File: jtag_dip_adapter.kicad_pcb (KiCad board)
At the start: 2 copper layers, 21.3 x 78.5 mm, 22 parts, among them J1 USB_B_Micro, J2 Conn_01x22, J3 Conn_01x22, J4 JTAG, J5 Conn_01x02, U1 MAX40203AUK+T, U2 74LVC1G04

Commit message: initial layout
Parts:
- added D3: BAT54W, Package_TO_SOT_SMD:SOT-323_SC-70, F.Cu at (134.1, 117.6)
- U2: value 74LVC1G04 -> 74HCT1G04
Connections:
- J5 pad 1: VCC -> Net-(D3-Pad1)
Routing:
- net VCC: track 0.00 -> 72.6 mm
- added copper zone on B.Cu, net GND
- added copper zone on F.Cu, net GND
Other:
- net class Default: clearance 0.2 -> 0.254; trace_width 0.25 -> 0.254; via_dia 0.8 -> 0.508; via_drill 0.4 -> 0.254
- net class Power added: clearance 0.254, trace_width 0.4064, via_dia 0.8128, via_drill 0.4064
- rule trace_clearance: 0.2 -> 0.254
- rule trace_min: 0.2 -> 0.1524
- rule via_min_drill: 0.3 -> 0.254
- rule via_min_size: 0.4 -> 0.508
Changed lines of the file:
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@@
     (thickness 1.6)
     (drawings 4)
-    (tracks 0)
+    (tracks 4)
     (zones 0)
-    (modules 22)
-    (nets 12)
+    (modules 23)
+    (nets 13)
   )
   (page A4)
@@
   )
   (setup
-    (last_trace_width 0.25)
-    (trace_clearance 0.2)
+    (last_trace_width 0.254)
+    (user_trace_width 0.254)
+    (user_trace_width 0.4064)
+    (trace_clearance 0.254)
     (zone_clearance 0.508)
     (zone_45_only no)
-    (trace_min 0.2)
-    (via_size 0.8)
-    (via_drill 0.4)
-    (via_min_size 0.4)
-    (via_min_drill 0.3)
+    (trace_min 0.1524)
+    (via_size 0.508)
+    (via_drill 0.254)
+    (via_min_size 0.508)
+    (via_min_drill 0.254)
+    (user_via 0.508 0.254)
+    (user_via 0.8128 0.4064)
     (uvia_size 0.3)
     (uvia_drill 0.1)
@@
     (pcb_text_width 0.3)
     (pcb_text_size 1.5 1.5)
-    (mod_edge_width 0.12)
-    (mod_text_size 1 1)
-    (mod_text_width 0.15)
+    (mod_edge_width 0.1524)
+    (mod_text_size 0.8128 0.8128)
+    (mod_text_width 0.1524)
     (pad_size 1.524 1.524)
     (pad_drill 0.762)
@@
   (net 10 /TCK)
   (net 11 /TDO)
+  (net 12 "Net-(D3-Pad1)")
   (net_class Default "This is the default net class."
-    (clearance 0.2)
-    (trace_width 0.25)
-    (via_dia 0.8)
-    (via_drill 0.4)
+    (clearance 0.254)
+    (trace_width 0.254)
+    (via_dia 0.508)
+    (via_drill 0.254)
     (uvia_dia 0.3)
     (uvia_drill 0.1)
@@
     (add_net /TDO)
     (add_net /TMS)
-    (add_net GND)
     (add_net "Net-(C1-Pad1)")
     (add_net "Net-(C3-Pad1)")
@@
     (add_net "Net-(D2-Pad1)")
     (add_net "Net-(D2-Pad2)")
+    (add_net "Net-(D3-Pad1)")
     (add_net "Net-(J1-Pad2)")
     (add_net "Net-(J1-Pad3)")
@@
     (add_net "Net-(J4-Pad8)")
     (add_net "Net-(U1-Pad4)")
+  )
+  (net_class Power ""
+    (clearance 0.254)
+    (trace_width 0.4064)
+    (via_dia 0.8128)
+    (via_drill 0.4064)
+    (uvia_dia 0.3)
+    (uvia_drill 0.1)
+    (add_net GND)
     (add_net VCC)
+  )
+  (module Package_TO_SOT_SMD:SOT-323_SC-70 (layer F.Cu)
+    (at 134.112 117.602)
+    (descr "SOT-323, SC-70")
+    (tags "SOT-323 SC-70")
+    (attr smd)
+    (fp_text reference D3 (at -0.05 -1.95) (layer F.SilkS)
+      (effects (font (size 1 1) (thickness 0.15)))
+    )
+    (fp_text value BAT54W (at -0.05 2.05) (layer F.Fab)
+      (effects (font (size 1 1) (thickness 0.15)))
+    )
+    (fp_line (start -0.18 -1.1) (end -0.68 -0.6) (layer F.Fab) (width 0.1))
+    (fp_line (start 0.67 1.1) (end -0.68 1.1) (layer F.Fab) (width 0.1))
+    (fp_line (start 0.67 -1.1) (end 0.67 1.1) (layer F.Fab) (width 0.1))
+    (fp_line (start -0.68 -0.6) (end -0.68 1.1) (layer F.Fab) (width 0.1))
+    (fp_line (start 0.67 -1.1) (end -0.18 -1.1) (layer F.Fab) (width 0.1))
+    (fp_line (start -0.68 1.16) (end 0.73 1.16) (layer F.SilkS) (width 0.12))
+    (fp_line (start 0.73 -1.16) (end -1.3 -1.16) (layer F.SilkS) (width 0.12))
+    (fp_line (start -1.7 1.3) (end -1.7 -1.3) (layer F.CrtYd) (width 0.05))
+    (fp_line (start -1.7 -1.3) (end 1.7 -1.3) (layer F.CrtYd) (width 0.05))
+    (fp_line (start 1.7 -1.3) (end 1.7 1.3) (layer F.CrtYd) (width 0.05))
+    (fp_line (start 1.7 1.3) (end -1.7 1.3) (layer F.CrtYd) (width 0.05))
+    (fp_line (start 0.73 -1.16) (end 0.73 -0.5) (layer F.SilkS) (width 0.12))
+    (fp_line (start 0.73 0.5) (end 0.73 1.16) (layer F.SilkS) (width 0.12))
+    (fp_text user %R (at 0 0 90) (layer F.Fab)
+      (effects (font (size 0.5 0.5) (thickness 0.075)))
+    )
+    (pad 3 smd rect (at 1 0 270) (size 0.45 0.7) (layers F.Cu F.Paste F.Mask)
+      (net 4 VCC))
+    (pad 2 smd rect (at -1 0.65 270) (size 0.45 0.7) (layers F.Cu F.Paste F.Mask))
+    (pad 1 smd rect (at -1 -0.65 270) (size 0.45 0.7) (layers F.Cu F.Paste F.Mask)
+      (net 12 "Net-(D3-Pad1)"))
+    (model ${KISYS3DMOD}/Package_TO_SOT_SMD.3dshapes/SOT-323_SC-70.wrl
+      (at (xyz 0 0 0))
+      (scale (xyz 1 1 1))
+      (rotate (xyz 0 0 0))
+    )
   )
   (module Connector_PinHeader_2.54mm:PinHeader_1x02_P2.54mm_Horizontal (layer F.Cu)
@@
       (net 1 GND))
     (pad 1 thru_hole rect (at 0 0 180) (size 1.7 1.7) (drill 1) (layers *.Cu *.Mask)
-      (net 4 VCC))
+      (net 12 "Net-(D3-Pad1)"))
     (model ${KISYS3DMOD}/Connector_PinHeader_2.54mm.3dshapes/PinHeader_1x02_P2.54mm_Horizontal.wrl
       (at (xyz 0 0 0))
@@
       (effects (font (size 1 1) (thickness 0.15)))
     )
-    (fp_text value 74LVC1G04 (at 0 2.5) (layer F.Fab)
+    (fp_text value 74HCT1G04 (at 0 2.5) (layer F.Fab)
       (effects (font (size 1 1) (thickness 0.15)))
     )
@@
   (gr_line (start 127 55.118) (end 148.336 55.118) (layer Edge.Cuts) (width 0.05))
   (gr_line (start 127 133.604) (end 127 55.118) (layer Edge.Cuts) (width 0.05))
+  (segment (start 130.048 77.724) (end 128.016 77.724) (width 0.4064) (layer F.Cu) (net 4))
+  (segment (start 128.016 77.724) (end 128.016 55.88) (width 0.4064) (layer F.Cu) (net 4))
+  (segment (start 128.016 77.724) (end 128.016 96.012) (width 0.4064) (layer F.Cu) (net 4))
+  (segment (start 128.016 96.012) (end 128.016 126.492) (width 0.4064) (layer F.Cu) (net 4))
+  (zone (net 1) (net_name GND) (layer F.Cu) (hatch edge 0.508)
+    (connect_pads (clearance 0.508))
+    (min_thickness 0.254)
+    (fill (arc_segments 32) (thermal_gap 0.508) (thermal_bridge_width 0.508))
+    (polygon
+      (pts
+        (xy 127 55.118) (xy 148.336 55.118) (xy 148.336 133.604) (xy 127 133.604)
+      )
+    )
+  )
+  (zone (net 1) (net_name GND) (layer B.Cu) (hatch edge 0.508)
+    (connect_pads (clearance 0.508))
+    (min_thickness 0.254)
+    (fill (arc_segments 32) (thermal_gap 0.508) (thermal_bridge_width 0.508))
+    (polygon
+      (pts
+        (xy 127 55.118) (xy 148.336 55.118) (xy 148.336 133.604) (xy 127.508 133.604) (xy 127 133.604)
+      )
+    )
+  )
 )

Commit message: finished routing and silkscreen
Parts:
- C1, C2, C4, C5, C6, C7, C8, D3, R3, U1, U2: moved to B.Cu
- moved D2 4.08 mm to (145.3, 121.2)
- moved R5 3.98 mm to (141.5, 121.2), turned to 180 degrees
- moved D3 3.57 mm to (133.9, 114.0)
- moved C1 3.30 mm to (134.1, 70.1)
- moved U2 2.97 mm to (142.5, 117.1)
- moved C2 2.40 mm to (141.5, 70.1)
- moved U1 2.34 mm to (137.2, 67.3)
- moved C4 2.30 mm to (133.9, 125.2)
- moved R1 1.41 mm to (140.2, 62.7)
- moved C3 1.02 mm to (135.1, 62.7)
- moved C8 0.29 mm to (141.5, 64.8)
- moved C6 0.25 mm to (133.9, 98.0)
- moved R2 0.25 mm to (133.9, 121.2)
- moved C7 0.14 mm to (141.5, 95.5)
- moved R4 0.14 mm to (141.5, 103.1)
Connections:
- J5 pad 1: Net-(D3-Pad1) -> GND
- J5 pad 2: GND -> Net-(D3-Pad1)
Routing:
- net /TDI: track 0.00 -> 80.7 mm, vias 0 -> 1
- net /TMS: track 0.00 -> 64.0 mm
- net /TDO: track 0.00 -> 55.7 mm
- net VCC: track 72.6 -> 126.2 mm, vias 0 -> 1
- net /TCK: track 0.00 -> 46.3 mm, vias 0 -> 2
- net GND: track 0.00 -> 22.9 mm, vias 0 -> 22
- net Net-(C3-Pad1): track 0.00 -> 17.2 mm
- net Net-(C1-Pad1): track 0.00 -> 14.5 mm, vias 0 -> 1
- net Net-(D2-Pad2): track 0.00 -> 6.81 mm, vias 0 -> 1
- net Net-(D3-Pad1): track 0.00 -> 2.87 mm
- net Net-(D2-Pad1): track 0.00 -> 2.06 mm
- net Net-(D1-Pad2): track 0.00 -> 2.06 mm
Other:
- rule pad_to_mask_clearance: 0.051 -> 0.0508
- rule solder_mask_min_width: 0.25 -> 0.1016
- board text added: "+5V"
- board text added: "1"
- board text added: "For 44 pin QFP and PLCC devices only with DIP adapter"
- board text added: "GND"
- board text added: "JTAG"
- board text added: "MAX7000S JTAG Adapter v1.0 by Hyiger Designs"
- board text added: "PWR"

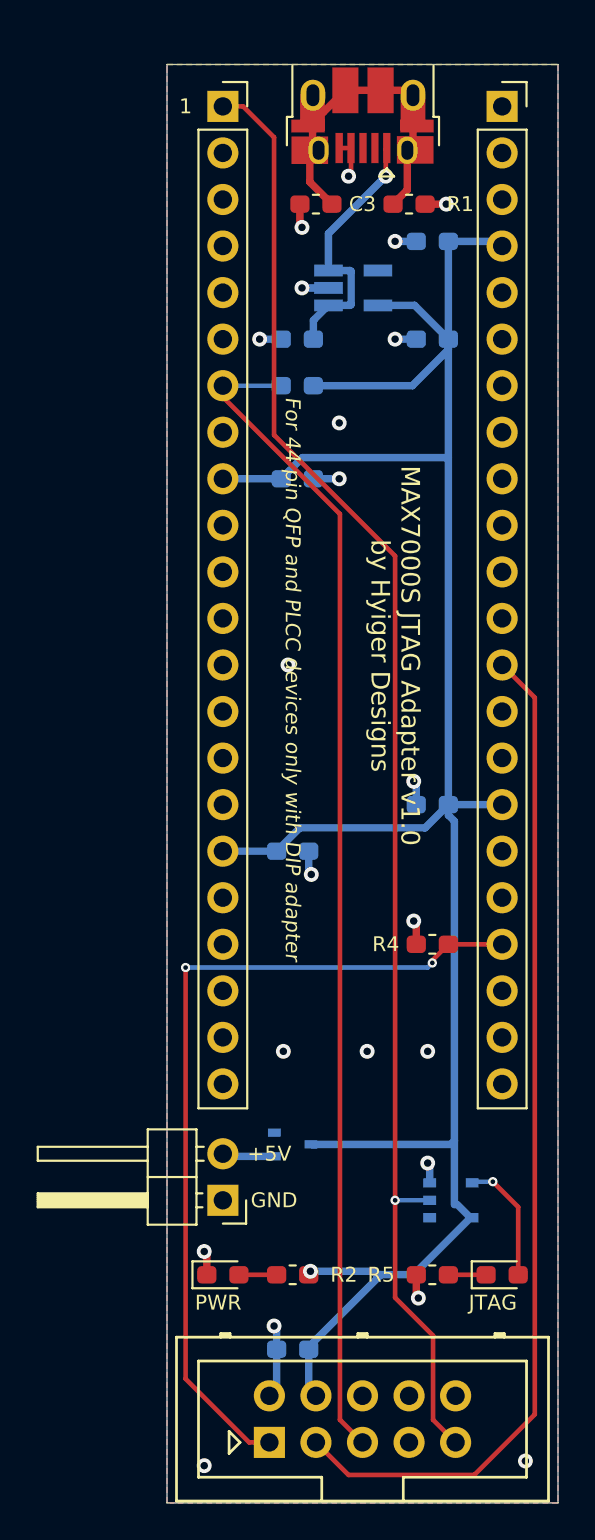
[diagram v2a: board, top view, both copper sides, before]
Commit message: added 5V ldo reg
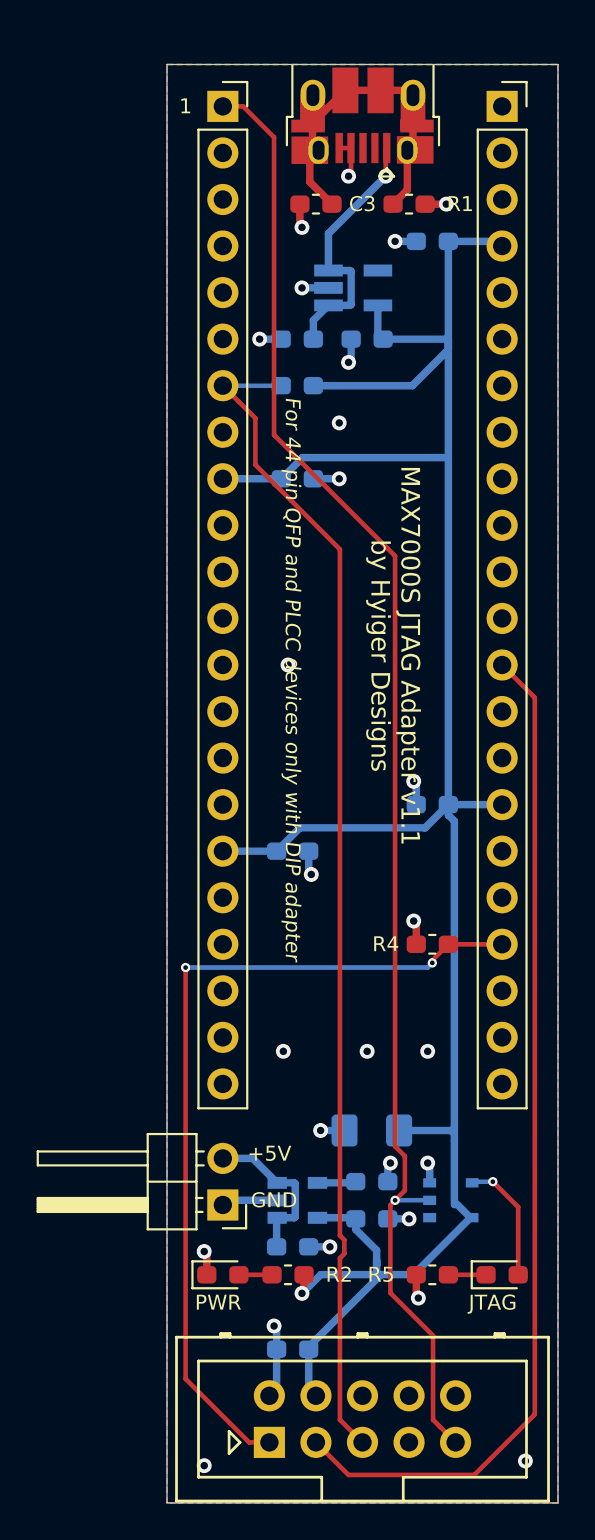
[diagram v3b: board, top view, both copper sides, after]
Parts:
- removed D3: BAT54W, Package_TO_SOT_SMD:SOT-323_SC-70
- removed J5: Conn_01x02, Connector_PinHeader_2.54mm:PinHeader_1x02_P2.54mm_Horizontal
- added C10: 10nF, Capacitor_SMD:C_0603_1608Metric_Pad1.05x0.95mm_HandSolder, B.Cu at (138.2, 116.1)
- added C11: 2.2uF, Capacitor_SMD:C_0603_1608Metric_Pad1.05x0.95mm_HandSolder, B.Cu at (138.2, 118.1)
- added C12: 100uF, Capacitor_SMD:C_1206_3216Metric_Pad1.42x1.75mm_HandSolder, B.Cu at (138.2, 113.3)
- added C9: 1uF, Capacitor_SMD:C_0603_1608Metric_Pad1.05x0.95mm_HandSolder, B.Cu at (133.9, 119.6)
- added J6: PWR, Connector_PinHeader_2.54mm:PinHeader_1x02_P2.54mm_Horizontal, F.Cu at (130.0, 117.3)
- added U3: LP2985-5.0, Package_TO_SOT_SMD:SOT-23-5, B.Cu at (134.1, 117.1)
- moved C2 3.56 mm to (137.9, 70.1)
- moved R2 0.25 mm to (133.6, 121.2)
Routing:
- net Net-(C9-Pad1): track 0.00 -> 9.14 mm
- net GND: track 22.9 -> 30.8 mm, vias 22 -> 26
- net VCC: track 126.2 -> 130.1 mm
- net Net-(D3-Pad1): track 2.87 -> 0.00 mm
- net Net-(C10-Pad1): track 0.00 -> 2.12 mm
- net /TDI: track 80.7 -> 81.3 mm
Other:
- board text added: "MAX7000S JTAG Adapter v1.1 by Hyiger Designs"
- board text removed: "MAX7000S JTAG Adapter v1.0 by Hyiger Designs"

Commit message: removed extra capacitor and vias
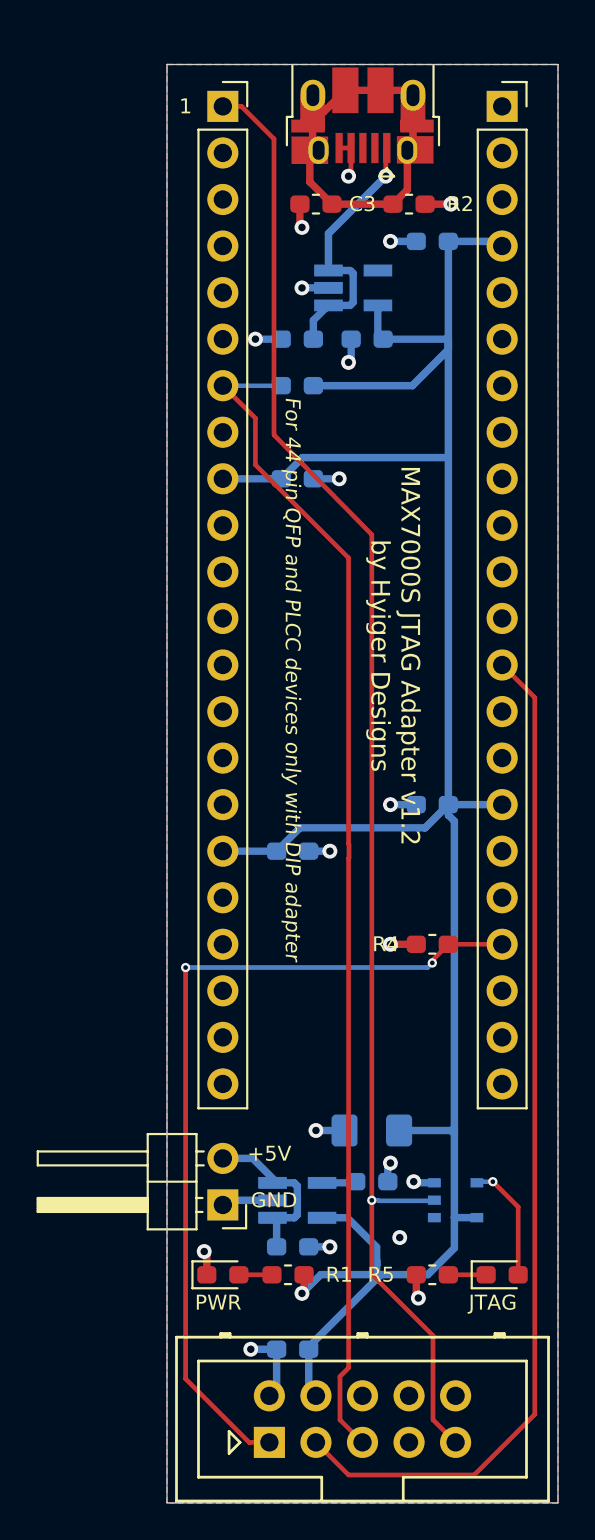
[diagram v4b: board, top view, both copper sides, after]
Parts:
- removed the C11 at (138.2, 118.1)
- removed the U2 at (142.5, 117.1)
- added U3: 74HCT1G04, Package_SO:TSOP-5_1.65x3.05mm_P0.95mm, B.Cu at (142.7, 117.1)
- U2: renamed from U3; value LP2985-5.0 -> LP2985-50DBVR; footprint Package_TO_SOT_SMD:SOT-23-5 -> Package_TO_SOT_SMD:SOT-23-5_HandSoldering
- renumbered C7 to C10, C8 to C11, C9 to C4, C10 to C5, C12 to C6, C4 to C7, C5 to C8, C6 to C9, J6 to J4, J4 to J5, R2 to R1, R1 to R2
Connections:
- J1 pad 2: (no net) -> Net-(J1-Pad2)
- J1 pad 3: (no net) -> Net-(J1-Pad3)
- J2 pad 10: (no net) -> Net-(J2-Pad10)
- J2 pad 11: (no net) -> Net-(J2-Pad11)
- J2 pad 12: (no net) -> Net-(J2-Pad12)
- J2 pad 13: (no net) -> Net-(J2-Pad13)
- J2 pad 14: (no net) -> Net-(J2-Pad14)
- J2 pad 15: (no net) -> Net-(J2-Pad15)
- J2 pad 18: (no net) -> Net-(J2-Pad18)
- J2 pad 19: (no net) -> Net-(J2-Pad19)
- J2 pad 2: (no net) -> Net-(J2-Pad2)
- J2 pad 20: (no net) -> Net-(J2-Pad20)
- J2 pad 21: (no net) -> Net-(J2-Pad21)
- J2 pad 22: (no net) -> Net-(J2-Pad22)
- J2 pad 3: (no net) -> Net-(J2-Pad3)
- J2 pad 5: (no net) -> Net-(J2-Pad5)
- J2 pad 6: (no net) -> Net-(J2-Pad6)
- J2 pad 8: (no net) -> Net-(J2-Pad8)
- J3 pad 1: (no net) -> Net-(J3-Pad1)
- J3 pad 10: (no net) -> Net-(J3-Pad10)
- J3 pad 11: (no net) -> Net-(J3-Pad11)
- J3 pad 12: (no net) -> Net-(J3-Pad12)
- J3 pad 14: (no net) -> Net-(J3-Pad14)
- J3 pad 15: (no net) -> Net-(J3-Pad15)
- J3 pad 17: (no net) -> Net-(J3-Pad17)
- J3 pad 18: (no net) -> Net-(J3-Pad18)
- J3 pad 2: (no net) -> Net-(J3-Pad2)
- J3 pad 20: (no net) -> Net-(J3-Pad20)
- J3 pad 22: (no net) -> Net-(J3-Pad22)
- J3 pad 3: (no net) -> Net-(J3-Pad3)
- J3 pad 5: (no net) -> Net-(J3-Pad5)
- J3 pad 6: (no net) -> Net-(J3-Pad6)
- J3 pad 7: (no net) -> Net-(J3-Pad7)
- J3 pad 8: (no net) -> Net-(J3-Pad8)
- J5 pad 6: (no net) -> Net-(J5-Pad6)
- J5 pad 7: (no net) -> Net-(J5-Pad7)
- J5 pad 8: (no net) -> Net-(J5-Pad8)
- U1 pad 4: (no net) -> Net-(U1-Pad4)
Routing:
- net Net-(C3-Pad1): track 17.2 -> 20.5 mm
- net VCC: track 130.1 -> 130.8 mm
- net /TDI: track 81.3 -> 81.9 mm
- net GND: track 30.8 -> 30.7 mm, vias 26 -> 19
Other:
- board text added: "MAX7000S JTAG Adapter v1.2 by Hyiger Designs"
- board text removed: "MAX7000S JTAG Adapter v1.1 by Hyiger Designs"
